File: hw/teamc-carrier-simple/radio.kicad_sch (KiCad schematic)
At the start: 6 parts, among them J30 SP4 breakout

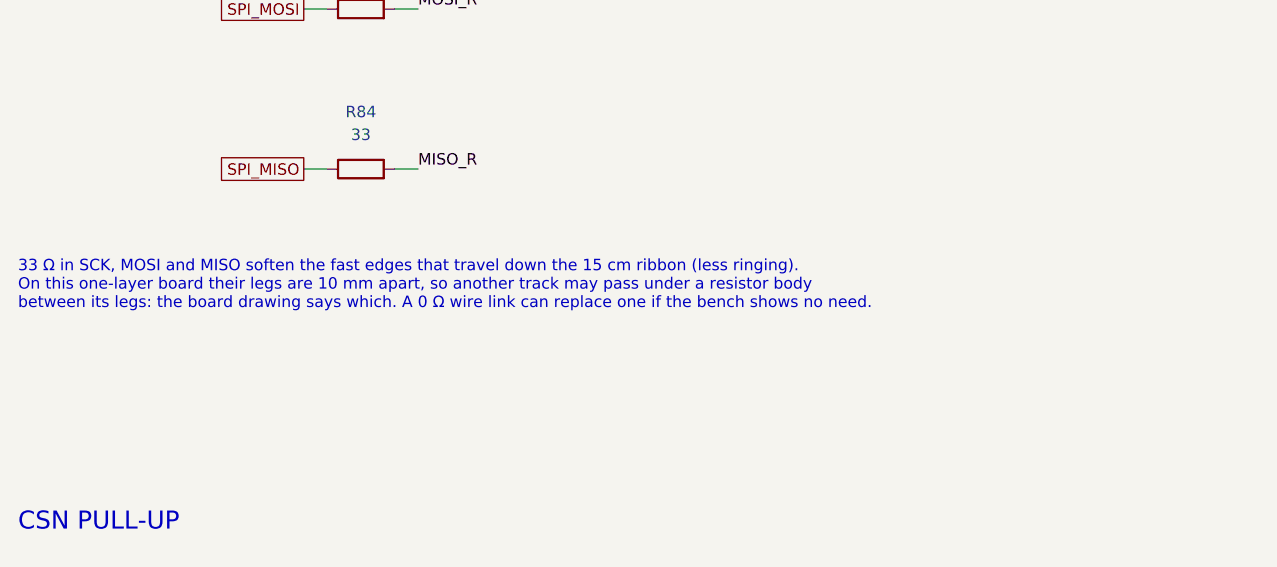
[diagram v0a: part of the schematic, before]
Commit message: Carrier rev C (simple): checkpoint 3 - placed and routed on one copper layer, DRC 0/0/0, 4 wire links
120 x 66 mm (box not measured yet: hw/scripts/layout_carrier_simple.py rebuilds everything after the
outline in place_carrier_simple.py changes). Backbone hand-routed (route_carrier_simple.py), router for
the short branches, GND pour; DRC with schematic parity 0 violations / 0 unconnected / 0 parity, all
severities; ERC 0/0. Tracks 0.8-2.0 mm. Wire links: IRQ over CSN and three ground pockets. Crossings by
tracks between resistor legs (SCK under R84/R83, LED_ACT_A under R61, CSN/IRQ under R57).
Layout-driven schematic changes: input 100 nF caps dropped, C18 at the toggle lead, 7.62 mm resistor
pitch, D1 on 12.7 mm, three M3 holes. Cable-tie slot + edge notch at the cell. 3D models for the
modules, wire links, holder, fuse clips and test points (gen_3d_revc.py; fetch_3d substitutes).
Fab: F.Cu + Edge.Cuts gerbers, drill, 1:1 copper PDFs, assembly PDFs, wire_links.csv, zip; renders.

Co-Authored-By: Claude Opus 5.5 <noreply@anthropic.com>
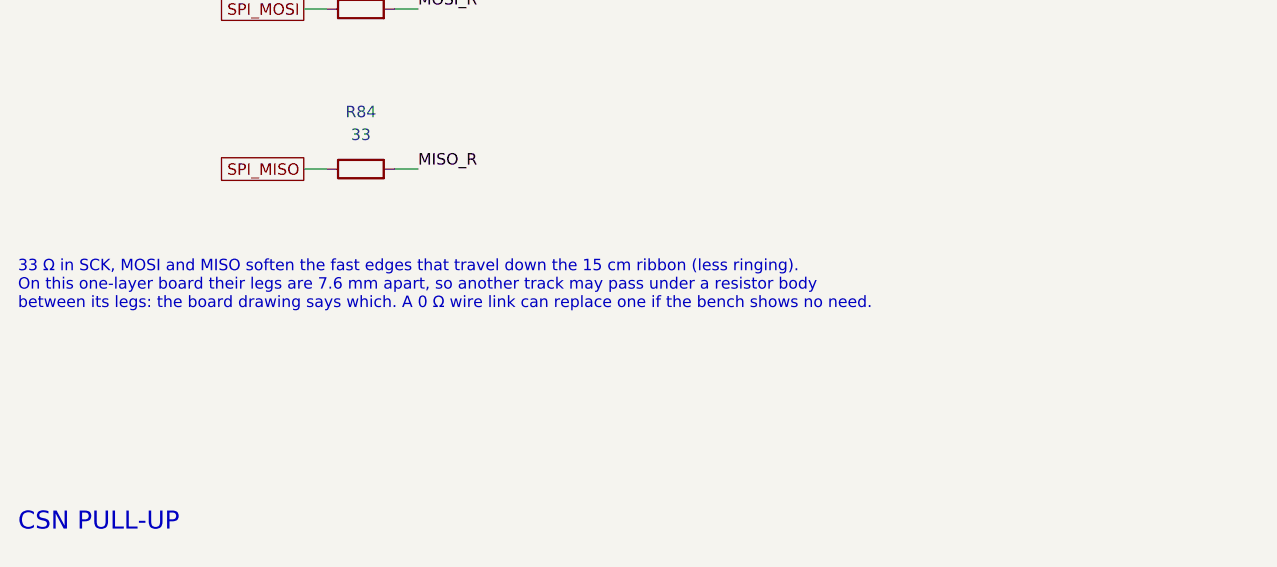
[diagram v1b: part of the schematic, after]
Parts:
- R80, R82, R83, R84: footprint teamc:R_Axial_DIN0207_L6.3mm_D2.5mm_P10.16mm_Horizontal_Pad1.8mm -> teamc:R_Axial_DIN0207_L6.3mm_D2.5mm_P7.62mm_Horizontal_Pad1.8mm
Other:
- note added: "33 Ω in SCK, MOSI and MISO soften the fast edges that travel down the 15 cm ribbon (less ringing). On this one-layer board their legs are 7.6 mm apart, so another track may pass under a resistor body between its legs: the board drawing says which. A 0 Ω wire link can replace one if the bench shows no need."
- note removed: "33 Ω in SCK, MOSI and MISO soften the fast edges that travel down the 15 cm ribbon (less ringing). On this one-layer board their legs are 10 mm apart, so another track may pass under a resistor body between its legs: the board drawing says which. A 0 Ω wire link can replace one if the bench shows no need."
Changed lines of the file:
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@@
 			)
 		)
-		(property "Footprint" "teamc:R_Axial_DIN0207_L6.3mm_D2.5mm_P10.16mm_Horizontal_Pad1.8mm"
+		(property "Footprint" "teamc:R_Axial_DIN0207_L6.3mm_D2.5mm_P7.62mm_Horizontal_Pad1.8mm"
 			(at 63.5 99.06 0)
 			(effects
@@
 			)
 		)
-		(property "Footprint" "teamc:R_Axial_DIN0207_L6.3mm_D2.5mm_P10.16mm_Horizontal_Pad1.8mm"
+		(property "Footprint" "teamc:R_Axial_DIN0207_L6.3mm_D2.5mm_P7.62mm_Horizontal_Pad1.8mm"
 			(at 63.5 116.84 0)
 			(effects
@@
 			)
 		)
-		(property "Footprint" "teamc:R_Axial_DIN0207_L6.3mm_D2.5mm_P10.16mm_Horizontal_Pad1.8mm"
+		(property "Footprint" "teamc:R_Axial_DIN0207_L6.3mm_D2.5mm_P7.62mm_Horizontal_Pad1.8mm"
 			(at 63.5 134.62 0)
 			(effects
@@
 			)
 		)
-		(property "Footprint" "teamc:R_Axial_DIN0207_L6.3mm_D2.5mm_P10.16mm_Horizontal_Pad1.8mm"
+		(property "Footprint" "teamc:R_Axial_DIN0207_L6.3mm_D2.5mm_P7.62mm_Horizontal_Pad1.8mm"
 			(at 63.5 190.5 0)
 			(effects
@@
 		)
 	)
-	(text "33 Ω in SCK, MOSI and MISO soften the fast edges that travel down the 15 cm ribbon (less ringing).\nOn this one-layer board their legs are 10 mm apart, so another track may pass under a resistor body\nbetween its legs: the board drawing says which. A 0 Ω wire link can replace one if the bench shows no need."
+	(text "33 Ω in SCK, MOSI and MISO soften the fast edges that travel down the 15 cm ribbon (less ringing).\nOn this one-layer board their legs are 7.6 mm apart, so another track may pass under a resistor body\nbetween its legs: the board drawing says which. A 0 Ω wire link can replace one if the bench shows no need."
 		(exclude_from_sim no)
 		(at 25.4 144.78 0)
